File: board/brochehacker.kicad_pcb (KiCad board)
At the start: 2 copper layers, 33 x 33.7 mm, 5 parts, among them IC1 ATTINY85-P, P1 CONN_01X02, U1 MAX7219

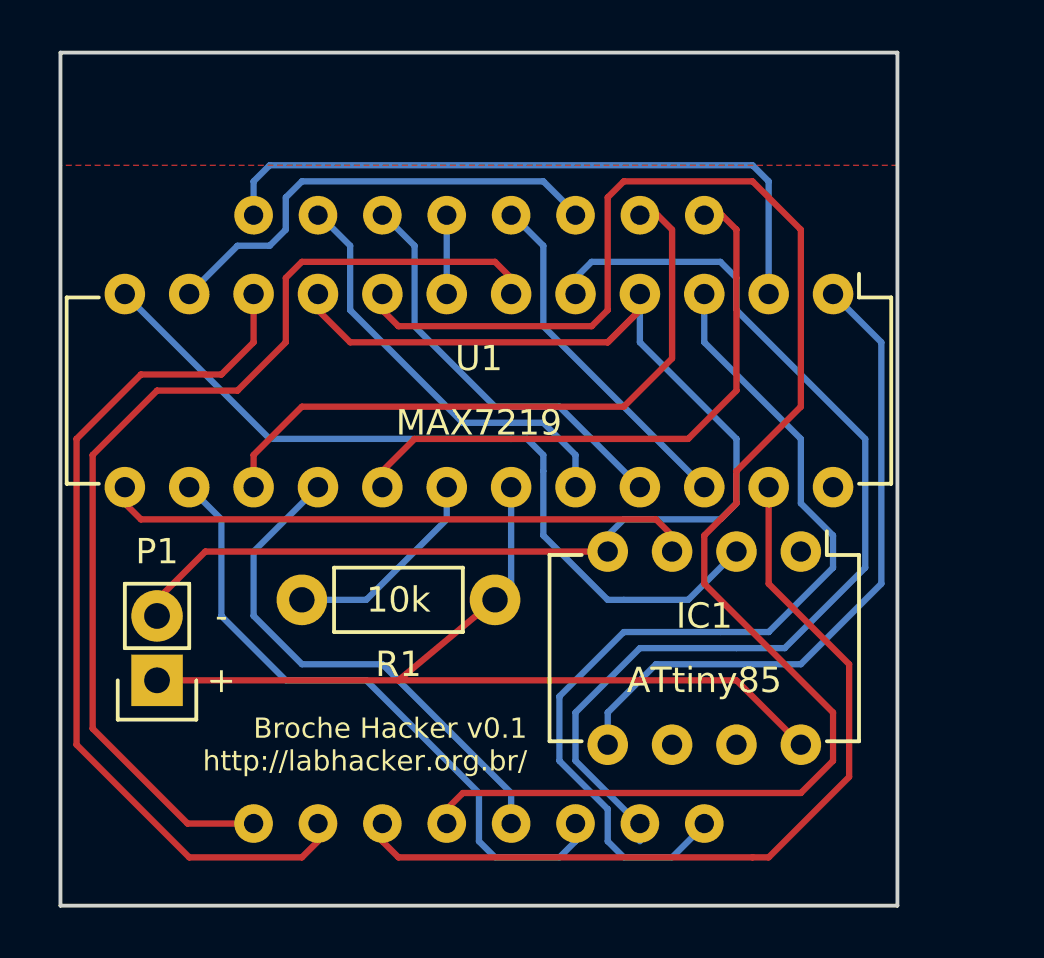
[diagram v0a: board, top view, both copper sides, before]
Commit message: move placa, mudanças em traços, silk, gerbers
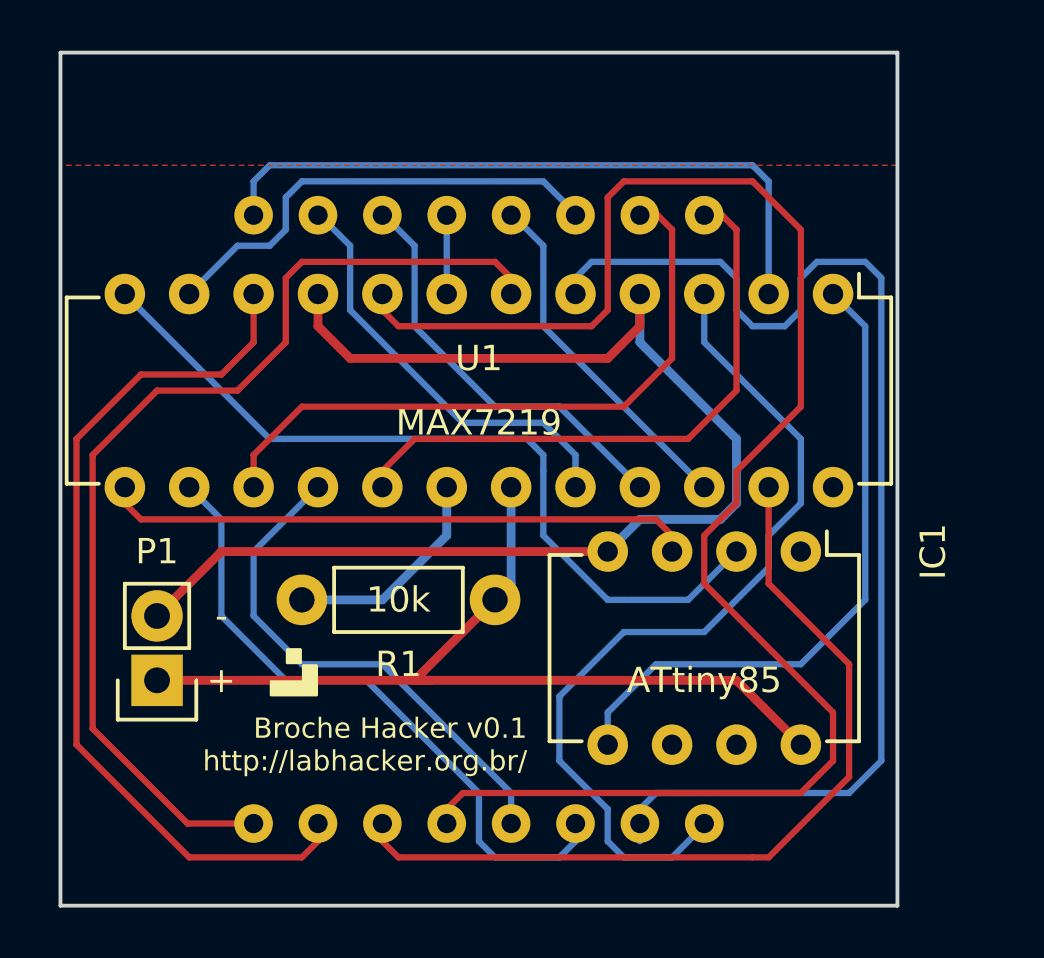
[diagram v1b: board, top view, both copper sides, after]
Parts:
- added ?: Symbol_OSHW-Logo_SilkScreen, oshw:Symbol_OSHW-Logo_SilkScreen, B.Cu at (188.0, 86.4)
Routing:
- net /DIG6: track 41.0 -> 47.5 mm
- net /DIG4: track 37.0 -> 34.5 mm
- net GND: track 54.0 -> 55.3 mm
- net VCC: track 37.9 -> 37.2 mm
- net Net-(IC1-Pad5): track 26.4 -> 25.9 mm
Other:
- net class Default: clearance 0.16 -> 0.2
- net class Power added: clearance 0.2, trace_width 0.35, via_dia 0.6, via_drill 0.4
- rule trace_clearance: 0.16 -> 0.2

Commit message: adição de chave de força
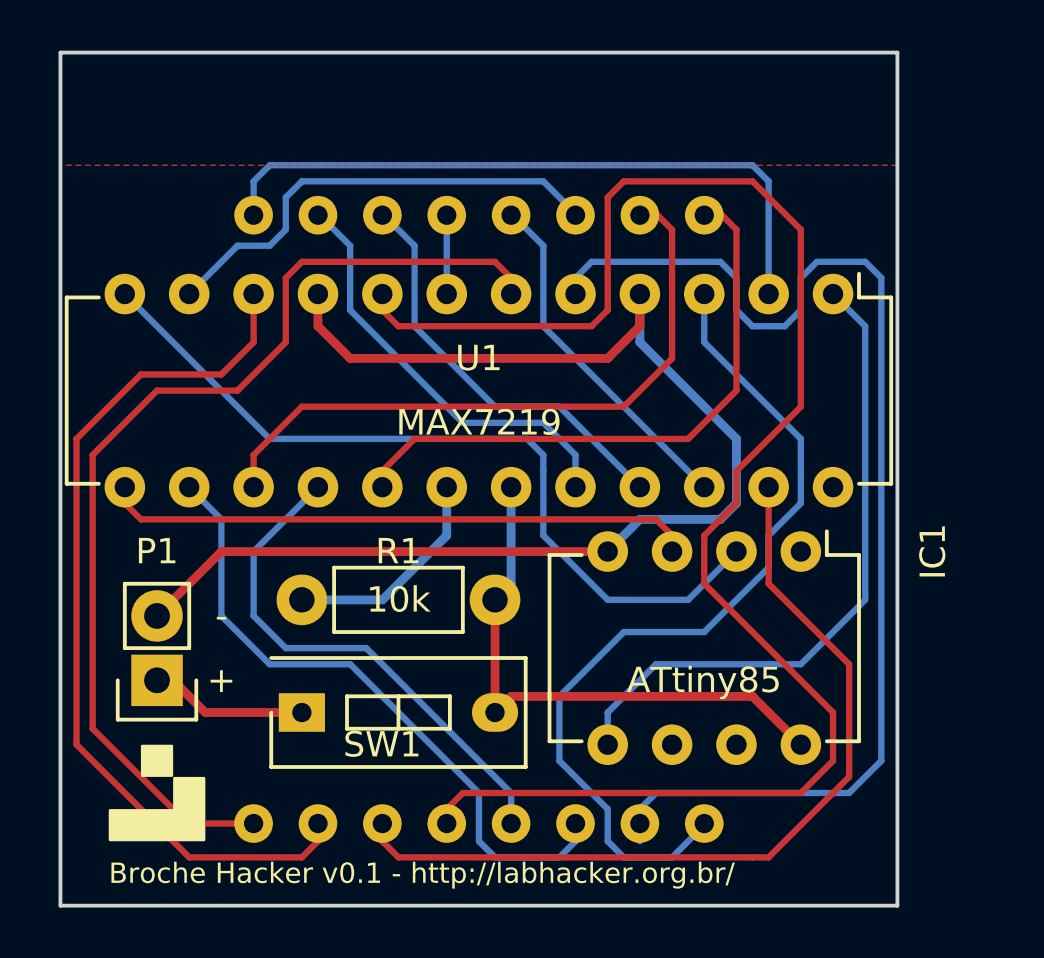
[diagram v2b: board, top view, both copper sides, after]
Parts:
- added SW1: SPST, Buttons_Switches_ThroughHole:SW_DIP_x1_Slide, F.Cu at (177.2, 109.2)
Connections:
- P1 pad 1: VCC -> Net-(P1-Pad1)
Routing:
- net VCC: track 37.2 -> 22.3 mm
- net Net-(P1-Pad1): track 0.00 -> 6.24 mm
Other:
- board text added: "Broche Hacker v0.1 - http://labhacker.org.br/"
- board text removed: "Broche Hacker v0.1 http://labhacker.org.br/"

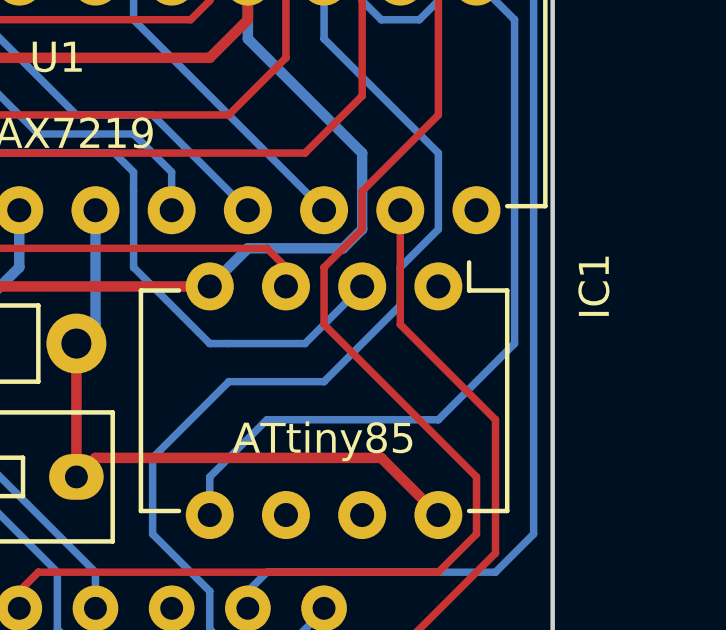
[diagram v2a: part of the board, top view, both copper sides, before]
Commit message: correção do silk
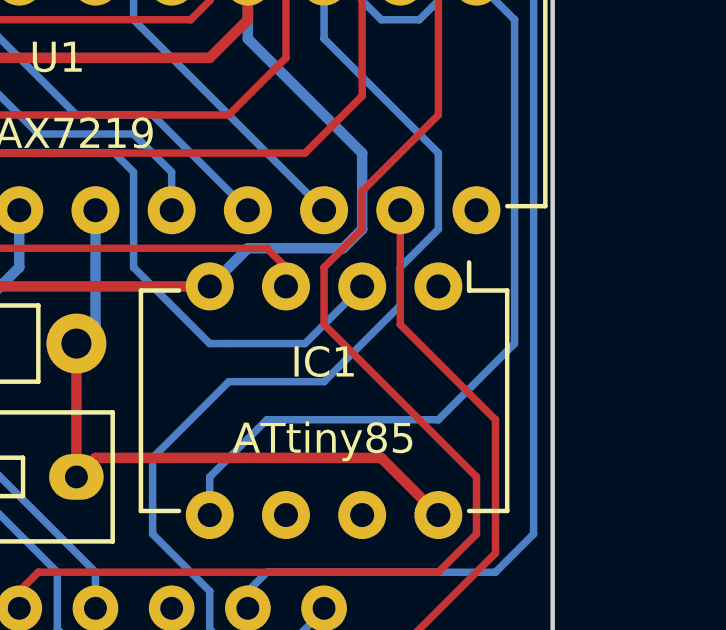
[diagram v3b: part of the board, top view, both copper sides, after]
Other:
- rule trace_min: 0.16 -> 0.25
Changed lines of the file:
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@@
     (zone_clearance 0.4)
     (zone_45_only no)
-    (trace_min 0.16)
+    (trace_min 0.25)
     (segment_width 0.2)
     (edge_width 0.15)
@@
     (descr "8-lead dip package, row spacing 7.62 mm (300 mils)")
     (tags "dil dip 2.54 300")
-    (fp_text reference IC1 (at 0 -5.22 270) (layer F.SilkS)
-      (effects (font (size 1 1) (thickness 0.15)))
-    )
+    (fp_text reference IC1 (at 2.54 3.81 360) (layer F.SilkS)
+      (effects (font (size 1 1) (thickness 0.15)))
+    )
